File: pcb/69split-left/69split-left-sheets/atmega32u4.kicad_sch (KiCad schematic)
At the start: 16 parts, among them J2 Conn_02x03_Odd_Even, SW1 SW_Push, U1 ATmega32U4-AU, Y1 Crystal

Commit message: Ordered the PCBs and parts!
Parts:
- C7, C8: MPN CC0603JRNPO0BN300 -> Generic
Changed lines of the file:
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@@
 			)
 		)
-		(property "MPN" "CC0603JRNPO0BN300 "
+		(property "MPN" "Generic"
 			(at 109.22 90.17 0)
 			(effects
@@
 			)
 		)
-		(property "MPN" "CC0603JRNPO0BN300 "
+		(property "MPN" "Generic"
 			(at 99.06 90.17 0)
 			(effects

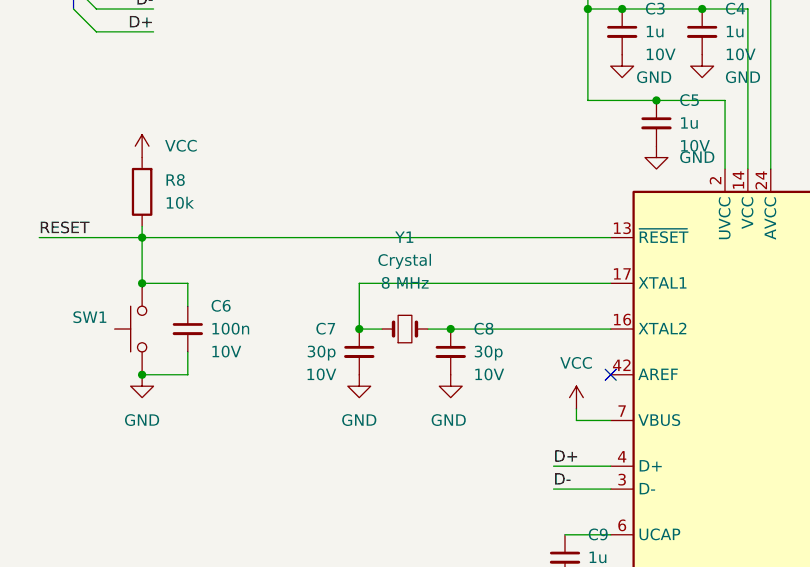
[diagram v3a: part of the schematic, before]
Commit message: Update crystal frequency and MPN
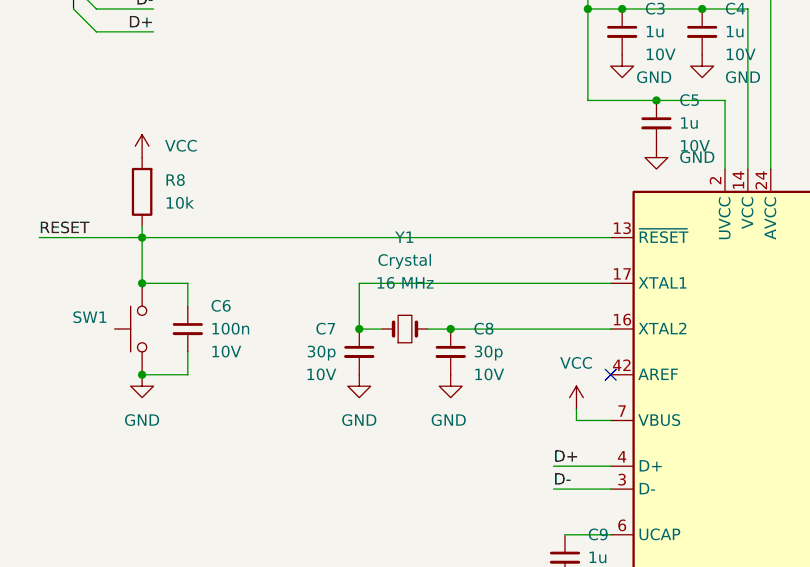
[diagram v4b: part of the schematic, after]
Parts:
- Y1: MPN ABL-8.000MHZ-B4Y-T -> ABL-16.000MHZ-B4Y-T; Rating 8 MHz -> 16 MHz
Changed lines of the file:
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@@
 			)
 		)
-		(property "MPN" "ABL-8.000MHZ-B4Y-T "
+		(property "MPN" "ABL-16.000MHZ-B4Y-T "
 			(at 104.14 87.63 0)
 			(hide yes)
@@
 			)
 		)
-		(property "Rating" "8 MHz"
+		(property "Rating" "16 MHz"
 			(at 104.14 82.55 0)
 			(show_name no)
